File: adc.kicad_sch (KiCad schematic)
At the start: 75 parts, among them CN1 100nF, CN2 100nF, CN3 100nF, CN4 100nF, U35 MCP6004, U36 MCP6004, U46 MCP6004, U8 MCP6004

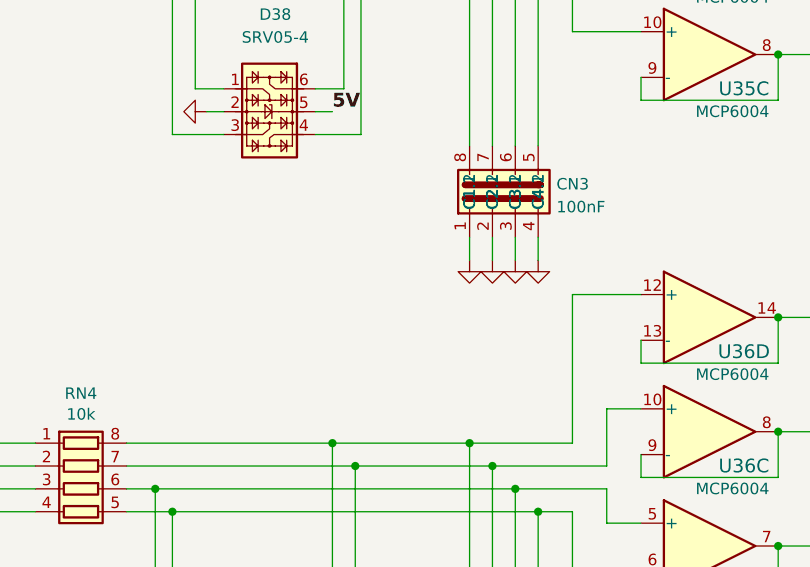
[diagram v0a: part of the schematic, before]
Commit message: added JP6
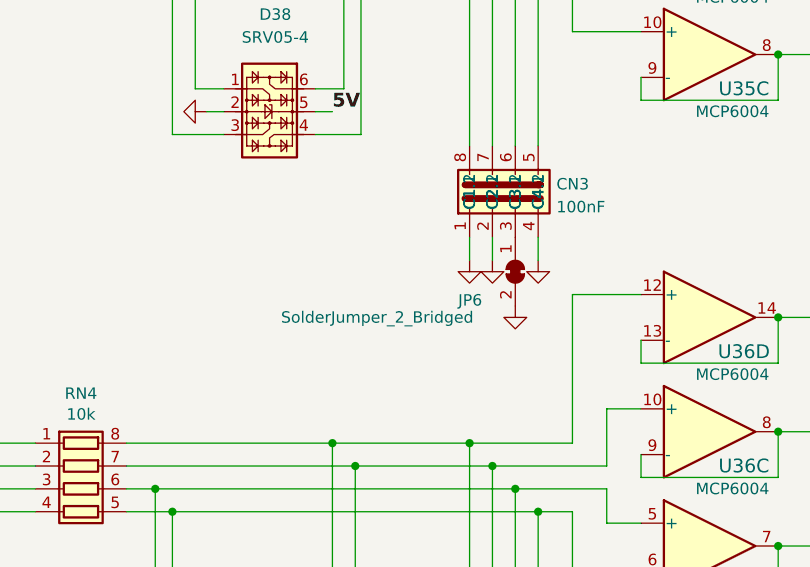
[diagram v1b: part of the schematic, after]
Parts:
- added JP6: SolderJumper_2_Bridged, Jumper:SolderJumper-2_P1.3mm_Bridged_RoundedPad1.0x1.5mm, symbol Jumper:SolderJumper_2_Bridged
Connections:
- net GND: now also JP6.2 (B); no longer CN3.3 (C3.1)
- new net: CN3.3 (C3.1), JP6.1 (A)
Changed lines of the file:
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@@
   (title_block
     (title "microRusEFI-2L")
-    (date "2023-01-19")
-    (rev "R0.6.1RC")
+    (date "2023-04-02")
+    (rev "R0.6.1rc")
     (company "rusEFI.com")
     (comment 1 "Donald Becker")
@@
     (stroke (width 0) (type default) (color 0 0 0 0))
   )
-  (wire (pts (xy 147.32 97.79) (xy 147.32 100.33))
-    (stroke (width 0) (type default) (color 0 0 0 0))
-  )
   (wire (pts (xy 146.05 217.17) (xy 146.05 220.98))
     (stroke (width 0) (type default) (color 0 0 0 0))
@@
     (pin "1")
   )
-  (symbol (lib_id "power:GND") (at 147.32 100.33 0) (unit 1)
+  (symbol (lib_id "power:GND") (at 147.32 105.41 0) (unit 1)
     (in_bom yes) (on_board yes)
-    (property "Reference" "#PWR0175" (id 0) (at 147.32 100.33 0)
+    (property "Reference" "#PWR0175" (id 0) (at 147.32 105.41 0)
       (effects (font (size 0.762 0.762)) hide)
     )
-    (property "Value" "GND" (id 1) (at 147.32 102.108 0)
+    (property "Value" "GND" (id 1) (at 147.32 107.188 0)
       (effects (font (size 0.762 0.762)) hide)
     )
-    (property "Footprint" "" (id 2) (at 147.32 100.33 0)
+    (property "Footprint" "" (id 2) (at 147.32 105.41 0)
       (effects (font (size 1.524 1.524)))
     )
-    (property "Datasheet" "" (id 3) (at 147.32 100.33 0)
+    (property "Datasheet" "" (id 3) (at 147.32 105.41 0)
       (effects (font (size 1.524 1.524)))
     )
@@
     (pin "8")
   )
+  (symbol (lib_id "Jumper:SolderJumper_2_Bridged") (at 147.32 101.6 270) (unit 1)
+    (in_bom yes) (on_board yes)
+    (property "Reference" "JP6" (id 0) (at 140.97 104.775 90)
+      (effects (font (size 1.27 1.27)) (justify left))
+    )
+    (property "Value" "SolderJumper_2_Bridged" (id 1) (at 121.285 106.68 90)
+      (effects (font (size 1.27 1.27)) (justify left))
+    )
+    (property "Footprint" "Jumper:SolderJumper-2_P1.3mm_Bridged_RoundedPad1.0x1.5mm" (id 2) (at 147.32 101.6 0)
+      (effects (font (size 1.27 1.27)) hide)
+    )
+    (property "Datasheet" "~" (id 3) (at 147.32 101.6 0)
+      (effects (font (size 1.27 1.27)) hide)
+    )
+    (pin "1")
+    (pin "2")
+  )
 )
